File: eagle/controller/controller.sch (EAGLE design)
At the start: 22 parts, among them IC1 ATMEGA48/88/168-PU, IC2 LP2950ACZ-5.0, K1 REED, K2 REED, K3 REED, Q1 BC517, Q2 BC517, Q3 BC517

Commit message: Change the irregular circle Q3
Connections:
- net GND: now also Q3.E
- net N$23: no longer Q3.E
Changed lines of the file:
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@@
 <junction x="279.4" y="-30.48"/>
 <junction x="287.02" y="-30.48"/>
-<wire x1="223.52" y1="-30.48" x2="223.52" y2="45.72" width="0.1524" layer="91"/>
+<wire x1="223.52" y1="-30.48" x2="223.52" y2="20.32" width="0.1524" layer="91"/>
 <junction x="223.52" y="-30.48"/>
 <pinref part="Q1" gate="G$1" pin="E"/>
+<wire x1="223.52" y1="20.32" x2="223.52" y2="45.72" width="0.1524" layer="91"/>
 <wire x1="223.52" y1="45.72" x2="223.52" y2="73.66" width="0.1524" layer="91"/>
 <wire x1="266.7" y1="68.58" x2="266.7" y2="73.66" width="0.1524" layer="91"/>
@@
 <junction x="223.52" y="45.72"/>
 <junction x="104.14" y="-7.62"/>
+<pinref part="Q3" gate="G$1" pin="E"/>
+<wire x1="266.7" y1="17.78" x2="266.7" y2="20.32" width="0.1524" layer="91"/>
+<wire x1="266.7" y1="20.32" x2="223.52" y2="20.32" width="0.1524" layer="91"/>
+<junction x="223.52" y="20.32"/>
 </segment>
 </net>
@@
 <wire x1="266.7" y1="5.08" x2="266.7" y2="7.62" width="0.1524" layer="91"/>
 <wire x1="254" y1="5.08" x2="228.6" y2="5.08" width="0.1524" layer="91"/>
-<wire x1="228.6" y1="5.08" x2="228.6" y2="20.32" width="0.1524" layer="91"/>
-<wire x1="228.6" y1="20.32" x2="228.6" y2="81.28" width="0.1524" layer="91"/>
+<wire x1="228.6" y1="5.08" x2="228.6" y2="81.28" width="0.1524" layer="91"/>
 <wire x1="228.6" y1="81.28" x2="160.02" y2="81.28" width="0.1524" layer="91"/>
 <wire x1="160.02" y1="81.28" x2="160.02" y2="53.34" width="0.1524" layer="91"/>
@@
 <wire x1="160.02" y1="53.34" x2="73.66" y2="53.34" width="0.1524" layer="91"/>
 <junction x="254" y="5.08"/>
-<pinref part="Q3" gate="G$1" pin="E"/>
-<wire x1="266.7" y1="17.78" x2="266.7" y2="20.32" width="0.1524" layer="91"/>
-<wire x1="266.7" y1="20.32" x2="228.6" y2="20.32" width="0.1524" layer="91"/>
-<junction x="228.6" y="20.32"/>
-</segment>
-</net>
+</segment>
+</net>

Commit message: Added Molex SDA connectors
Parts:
- added X1, X2, X3: 43160-1102, con-molex:43160-1102
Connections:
- net N$10: now also X2-2.S@1
- net N$11: now also X3-2.S@1
- net N$15: now also X1-1.S@1
- net N$16: now also X2-1.S@1
- net N$17: now also X3-1.S@1
- net N$9: now also X1-2.S@1
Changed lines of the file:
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@@
 <part name="R9" library="resistor" deviceset="R-EU_" device="0204/7" value="10k"/>
 <part name="R10" library="resistor" deviceset="R-EU_" device="0204/7" value="10k"/>
+<part name="X1" library="con-molex" deviceset="43160-*02" device="" technology="11"/>
+<part name="X2" library="con-molex" deviceset="43160-*02" device="" technology="11"/>
+<part name="X3" library="con-molex" deviceset="43160-*02" device="" technology="11"/>
 </parts>
 <sheets>
@@
 <instance part="R9" gate="G$1" x="243.84" y="63.5" rot="R270"/>
 <instance part="R10" gate="G$1" x="254" y="12.7" rot="R90"/>
+<instance part="X1" gate="-1" x="353.06" y="55.88"/>
+<instance part="X1" gate="-2" x="353.06" y="53.34"/>
+<instance part="X2" gate="-1" x="353.06" y="30.48"/>
+<instance part="X2" gate="-2" x="353.06" y="27.94"/>
+<instance part="X3" gate="-1" x="353.06" y="7.62"/>
+<instance part="X3" gate="-2" x="353.06" y="5.08"/>
 </instances>
 <busses>
@@
 <pinref part="K3" gate="2" pin="P"/>
 <wire x1="205.74" y1="53.34" x2="205.74" y2="48.26" width="0.1524" layer="91"/>
-<wire x1="205.74" y1="48.26" x2="330.2" y2="48.26" width="0.1524" layer="91"/>
+<wire x1="205.74" y1="48.26" x2="347.98" y2="48.26" width="0.1524" layer="91"/>
+<pinref part="X1" gate="-2" pin="S@1"/>
+<wire x1="347.98" y1="48.26" x2="347.98" y2="53.34" width="0.1524" layer="91"/>
 </segment>
 </net>
@@
 <pinref part="K2" gate="2" pin="P"/>
 <wire x1="205.74" y1="30.48" x2="205.74" y2="25.4" width="0.1524" layer="91"/>
-<wire x1="205.74" y1="25.4" x2="330.2" y2="25.4" width="0.1524" layer="91"/>
+<wire x1="205.74" y1="25.4" x2="347.98" y2="25.4" width="0.1524" layer="91"/>
+<pinref part="X2" gate="-2" pin="S@1"/>
+<wire x1="347.98" y1="25.4" x2="347.98" y2="27.94" width="0.1524" layer="91"/>
 </segment>
 </net>
@@
 <pinref part="K1" gate="2" pin="P"/>
 <wire x1="205.74" y1="7.62" x2="205.74" y2="2.54" width="0.1524" layer="91"/>
-<wire x1="205.74" y1="2.54" x2="330.2" y2="2.54" width="0.1524" layer="91"/>
+<wire x1="205.74" y1="2.54" x2="347.98" y2="2.54" width="0.1524" layer="91"/>
+<pinref part="X3" gate="-2" pin="S@1"/>
+<wire x1="347.98" y1="2.54" x2="347.98" y2="5.08" width="0.1524" layer="91"/>
 </segment>
 </net>
@@
 <segment>
 <pinref part="R4" gate="G$1" pin="2"/>
-<wire x1="307.34" y1="60.96" x2="330.2" y2="60.96" width="0.1524" layer="91"/>
+<wire x1="307.34" y1="60.96" x2="347.98" y2="60.96" width="0.1524" layer="91"/>
+<pinref part="X1" gate="-1" pin="S@1"/>
+<wire x1="347.98" y1="60.96" x2="347.98" y2="55.88" width="0.1524" layer="91"/>
 </segment>
 </net>
@@
 <segment>
 <pinref part="R3" gate="G$1" pin="2"/>
-<wire x1="307.34" y1="35.56" x2="330.2" y2="35.56" width="0.1524" layer="91"/>
+<wire x1="307.34" y1="35.56" x2="347.98" y2="35.56" width="0.1524" layer="91"/>
+<pinref part="X2" gate="-1" pin="S@1"/>
+<wire x1="347.98" y1="35.56" x2="347.98" y2="30.48" width="0.1524" layer="91"/>
 </segment>
 </net>
@@
 <segment>
 <pinref part="R2" gate="G$1" pin="2"/>
-<wire x1="307.34" y1="10.16" x2="330.2" y2="10.16" width="0.1524" layer="91"/>
-</segment>
-</net>
+<wire x1="307.34" y1="10.16" x2="347.98" y2="10.16" width="0.1524" layer="91"/>
+<pinref part="X3" gate="-1" pin="S@1"/>
+<wire x1="347.98" y1="10.16" x2="347.98" y2="7.62" width="0.1524" layer="91"/>
+</segment>
+</net>

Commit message: Relais and power supply
- Correct powersupply to USB
- Added 230V AC relais
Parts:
- added B1, B2, B3: (no value), e-messfuehler:MESSFUEHLER_2
- added F1: (no value), e-sicherungen:SICHERUNG_1-POL
- added K6: (no value), e-schuetze-relais:HILFSSCHUETZ_13-14
- added POWER230V, X5: C-GRID-02-15-19, con-molex:C-GRID-02-15-19
- added X4: (no value), con-berg:PN87520
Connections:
- new net N$1: IC4.O4, K6G$1.A2
- new net N$20: B1.2
- new net N$21: B1.1
- new net N$24: B2.2
- new net N$25: B2.1
- new net N$26: B3.2
- new net N$27: B3.1
- new net N$28: F1.2, K61.3
- new net N$30: K61.4, POWER230V-2.S, X5-2.S
- new net N$32: F1.1, POWER230V-1.S, X5-1.S
- net +5V: now also X4.1
- net GND: now also X4.4
- net N$18: now also K6G$1.A1

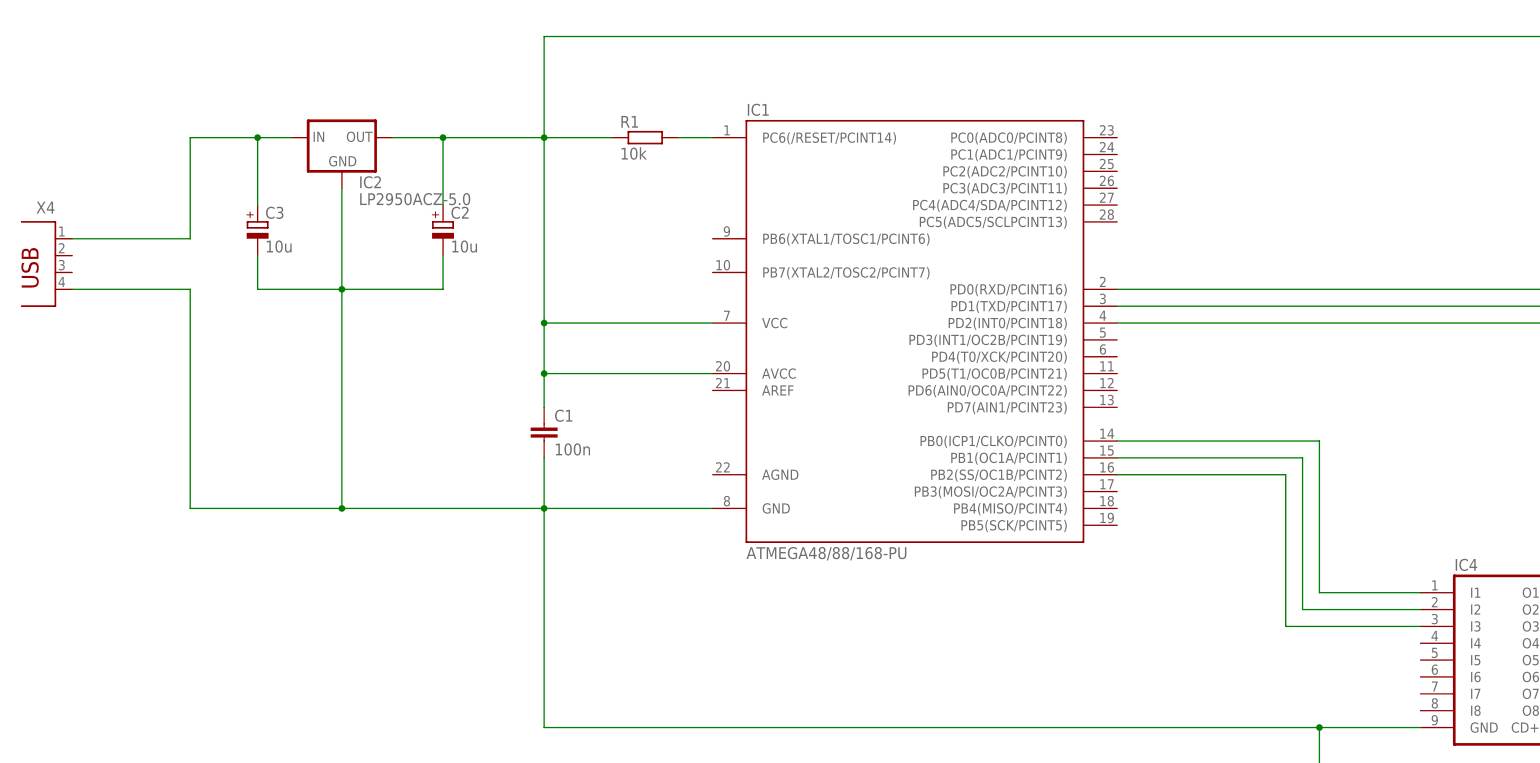
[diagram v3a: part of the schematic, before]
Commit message: Optimized the power supply
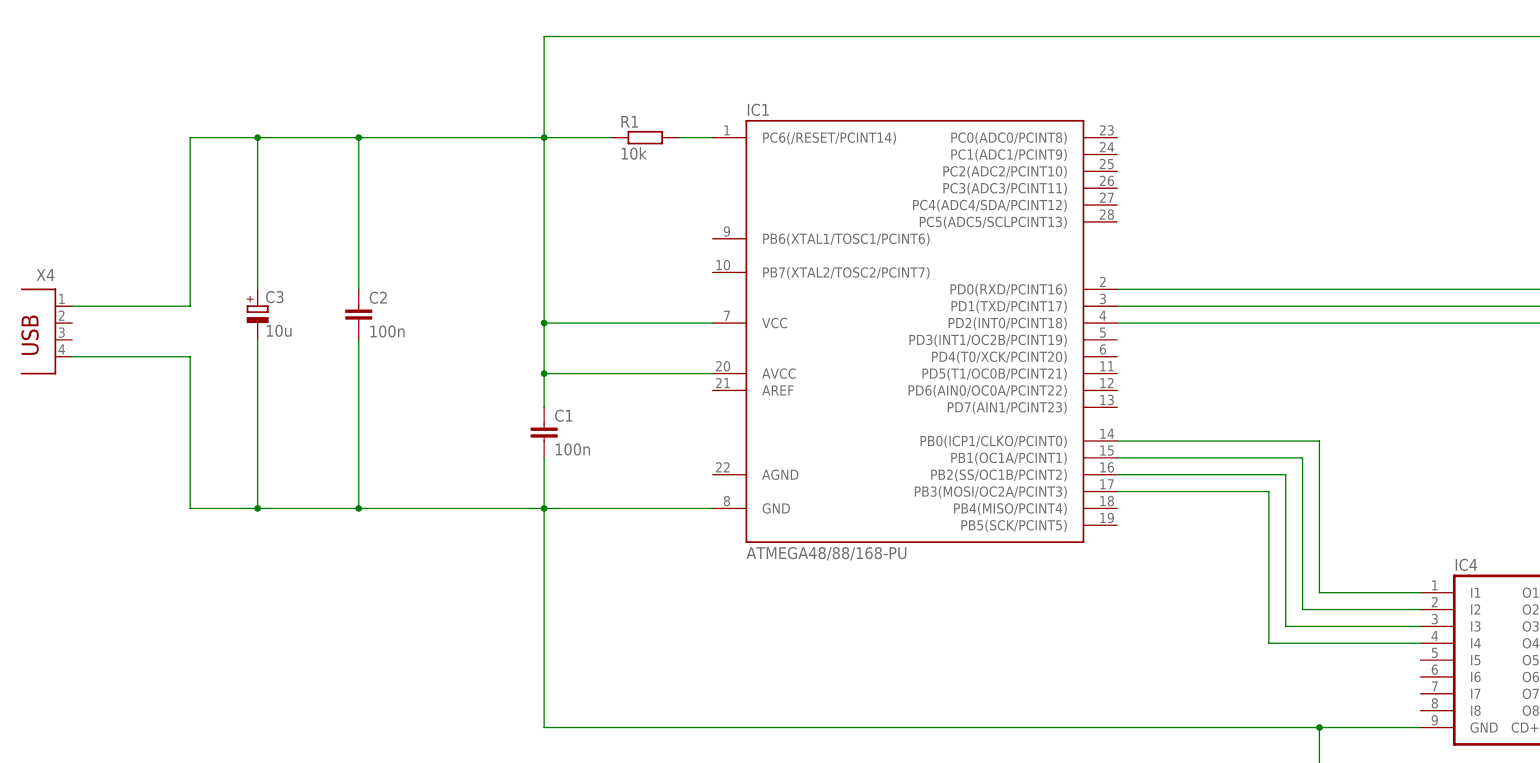
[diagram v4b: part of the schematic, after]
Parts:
- removed IC2: LP2950ACZ-5.0, v-reg:LP2950ACZ-5.0
- C2: value 10u -> 100n; device resistor:CPOL-EUE2.5-7 -> resistor:C-EU025-030X050
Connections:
- removed net N$18: C1.1, C2.+, IC1.AVCC, IC1.VCC@1, IC2.OUT, IC4.CD+, K11.+, K12.S, K21.+, K22.S, K31.+, K32.S, K6G$1.A1, R1.1, R10.2, R8.2, R9.1
- new net N$29: IC1.PB3(MOSI/OC2A/PCINT3), IC4.I4
- net +5V: now also C1.1, C2.1, IC1.AVCC, IC1.VCC@1, IC4.CD+, K11.+, K12.S, K21.+, K22.S, K31.+, K32.S, K6G$1.A1, R1.1, R10.2, R8.2, R9.1; no longer IC2.IN
- net GND: now also C2.2; no longer C2.-, IC2.GND
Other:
- moved on the sheet: C3, X4

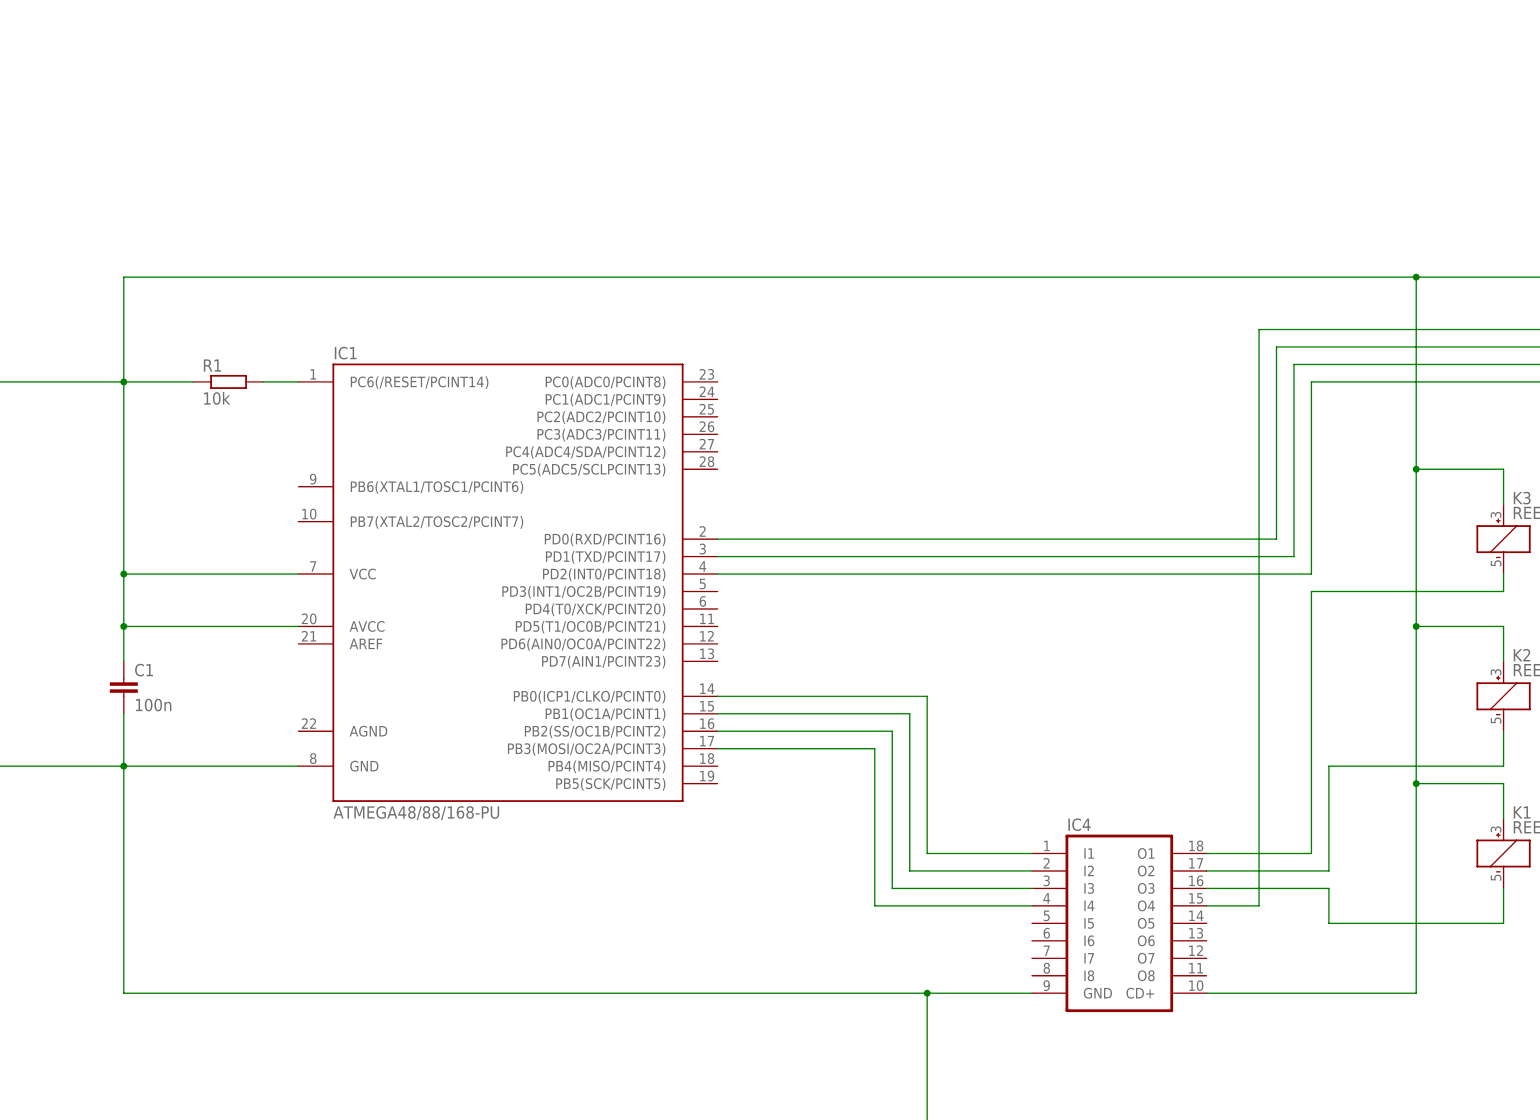
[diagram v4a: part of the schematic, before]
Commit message: Added programmer interface
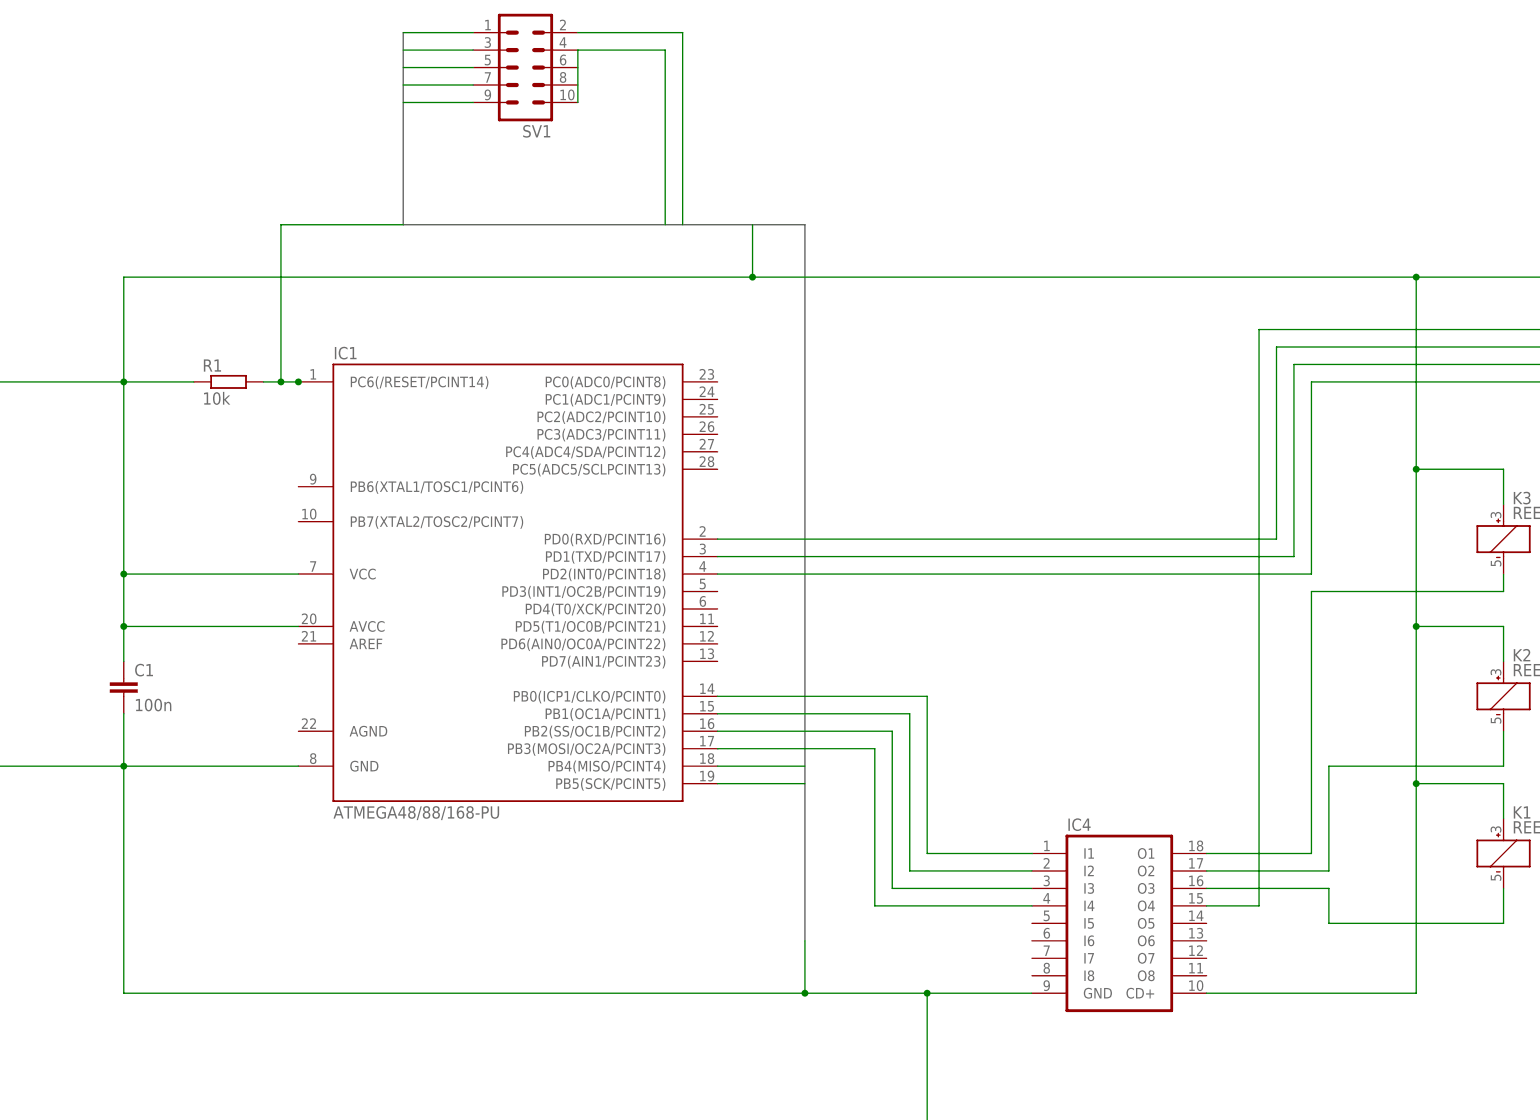
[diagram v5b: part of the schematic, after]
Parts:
- added SV1: (no value), con-lstb:MA05-2
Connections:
- net +5V renamed VCC
- removed net N$2: IC1.PC6(/RESET/PCINT14), R1.2
- removed net N$29: IC1.PB3(MOSI/OC2A/PCINT3), IC4.I4
- new net LED: SV1.3
- new net MISO: IC1.PB4(MISO/PCINT4), SV1.9
- new net MOSI: IC1.PB3(MOSI/OC2A/PCINT3), IC4.I4, SV1.1
- new net RESET: IC1.PC6(/RESET/PCINT14), R1.2, SV1.5
- new net SCK: IC1.PB5(SCK/PCINT5), SV1.7
- net GND: now also SV1.10, SV1.2, SV1.4

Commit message: Added LED for programming feedback
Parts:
- added LED1: (no value), led:LED5MM
- added R11: 470, resistor:R-EU_0204/7
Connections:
- new net N$2: LED1.A, R11.2
- net LED: now also LED1.C
- net VCC: now also R11.1
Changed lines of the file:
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@@
 <part name="C2" library="resistor" deviceset="C-EU" device="025-030X050" value="100n"/>
 <part name="SV1" library="con-lstb" deviceset="MA05-2" device=""/>
+<part name="LED1" library="led" deviceset="LED" device="5MM"/>
+<part name="R11" library="resistor" deviceset="R-EU_" device="0204/7" value="470"/>
 </parts>
 <sheets>
@@
 <instance part="C2" gate="G$1" x="-40.64" y="55.88"/>
 <instance part="SV1" gate="G$1" x="45.72" y="127" rot="R180"/>
+<instance part="LED1" gate="G$1" x="2.54" y="116.84" rot="R90"/>
+<instance part="R11" gate="G$1" x="-7.62" y="106.68" rot="R90"/>
 </instances>
 <busses>
@@
 <wire x1="38.1" y1="129.54" x2="27.94" y2="129.54" width="0.1524" layer="91"/>
 </segment>
+<segment>
+<pinref part="LED1" gate="G$1" pin="C"/>
+<wire x1="7.62" y1="116.84" x2="27.94" y2="116.84" width="0.1524" layer="91"/>
+</segment>
 </net>
 <net name="RESET" class="0">
@@
 <junction x="-12.7" y="45.72"/>
 <wire x1="-12.7" y1="81.28" x2="-12.7" y2="96.52" width="0.1524" layer="91"/>
-<wire x1="-12.7" y1="96.52" x2="78.74" y2="96.52" width="0.1524" layer="91"/>
+<wire x1="-12.7" y1="96.52" x2="-7.62" y2="96.52" width="0.1524" layer="91"/>
+<wire x1="-7.62" y1="96.52" x2="78.74" y2="96.52" width="0.1524" layer="91"/>
 <wire x1="78.74" y1="96.52" x2="175.26" y2="96.52" width="0.1524" layer="91"/>
 <wire x1="175.26" y1="96.52" x2="175.26" y2="68.58" width="0.1524" layer="91"/>
@@
 <wire x1="78.74" y1="104.14" x2="78.74" y2="96.52" width="0.1524" layer="91"/>
 <junction x="78.74" y="96.52"/>
-</segment>
-</net>
+<pinref part="R11" gate="G$1" pin="1"/>
+<wire x1="-7.62" y1="96.52" x2="-7.62" y2="101.6" width="0.1524" layer="91"/>
+</segment>
+</net>
+<net name="N$2" class="0">
+<segment>
+<pinref part="R11" gate="G$1" pin="2"/>
+<pinref part="LED1" gate="G$1" pin="A"/>
+<wire x1="-7.62" y1="111.76" x2="-7.62" y2="116.84" width="0.1524" layer="91"/>
+<wire x1="-7.62" y1="116.84" x2="0" y2="116.84" width="0.1524" layer="91"/>
+</segment>
+</net>
